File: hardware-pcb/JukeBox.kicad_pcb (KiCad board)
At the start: 2 copper layers, 93.8 x 90 mm, 82 parts, among them J1 USB4105-GF-A, J2 Conn_01x04_Pin, Q1 Q_NPN_BEC, SW1 SW_SPST, SW10 SW_SPST, SW11 SW_SPST, SW12 SW_SPST, SW2 SW_SPST, SW3 SW_SPST, SW4 SW_SPST, SW5 SW_SPST, SW6 SW_SPST, SW7 SW_SPST, SW8 SW_SPST, SW9 SW_SPST, U1 NCP1117-3.3_SOT223, U2 W25Q64JVSSIQ-TR, U3 RP2040, U4 st7789v, U5 CAT24C512, Y1 ECS-120-20-33-AEL-TR

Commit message: minor eeprom updates
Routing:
- net /GPIO4: track 92.0 -> 92.9 mm
- net /GPIO5: track 92.8 -> 93.3 mm
- net GND: vias 35 -> 43
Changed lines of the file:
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@@
 		(tags "SOIC SO")
 		(property "Reference" "U5"
-			(at 0 0 360)
+			(at 0 0 0)
 			(layer "F.SilkS")
 			(effects
@@
 		)
 		(property "Value" "CAT24C512"
-			(at 0 3.4 360)
+			(at 0 3.4 0)
 			(layer "F.Fab")
 			(effects
@@
 		)
 		(fp_text user "${REFERENCE}"
-			(at 0 0 360)
+			(at 0 0 0)
 			(layer "F.Fab")
 			(effects
@@
 	)
 	(via
+		(at 102.59 141.85)
+		(size 0.6)
+		(drill 0.35)
+		(layers "F.Cu" "B.Cu")
+		(free yes)
+		(net 1)
+	)
+	(via
 		(at 112.59 131.85)
 		(size 0.6)
@@
 	)
 	(via
+		(at 122.59 141.85)
+		(size 0.6)
+		(drill 0.35)
+		(layers "F.Cu" "B.Cu")
+		(free yes)
+		(net 1)
+	)
+	(via
 		(at 89.09 94.75)
 		(size 0.6)
@@
 	)
 	(via
+		(at 82.59 121.85)
+		(size 0.6)
+		(drill 0.35)
+		(layers "F.Cu" "B.Cu")
+		(free yes)
+		(net 1)
+	)
+	(via
 		(at 70.09 111.85)
 		(size 0.6)
@@
 	)
 	(via
+		(at 102.59 121.85)
+		(size 0.6)
+		(drill 0.35)
+		(layers "F.Cu" "B.Cu")
+		(free yes)
+		(net 1)
+	)
+	(via
 		(at 155.09 151.85)
 		(size 0.6)
@@
 	)
 	(via
+		(at 82.59 141.85)
+		(size 0.6)
+		(drill 0.35)
+		(layers "F.Cu" "B.Cu")
+		(free yes)
+		(net 1)
+	)
+	(via
 		(at 92.59 131.85)
 		(size 0.6)
@@
 	)
 	(via
+		(at 142.59 141.85)
+		(size 0.6)
+		(drill 0.35)
+		(layers "F.Cu" "B.Cu")
+		(free yes)
+		(net 1)
+	)
+	(via
 		(at 132.59 131.85)
 		(size 0.6)
@@
 	)
 	(via
+		(at 122.59 121.85)
+		(size 0.6)
+		(drill 0.35)
+		(layers "F.Cu" "B.Cu")
+		(free yes)
+		(net 1)
+	)
+	(via
+		(at 142.59 121.85)
+		(size 0.6)
+		(drill 0.35)
+		(layers "F.Cu" "B.Cu")
+		(free yes)
+		(net 1)
+	)
+	(via
 		(at 112.59 111.85)
 		(size 0.6)
@@
 	)
 	(segment
-		(start 82.725 100.865)
+		(start 82.225 100.865)
 		(end 83.615 100.865)
 		(width 0.15)
@@
 	)
 	(segment
-		(start 81.84 101.75)
-		(end 82.725 100.865)
+		(start 75.639999 104.799999)
+		(end 77.540001 104.799999)
 		(width 0.15)
 		(layer "F.Cu")
@@
 	)
 	(segment
-		(start 75.639999 104.799999)
-		(end 77.540001 104.799999)
+		(start 75.34 104.5)
+		(end 75.639999 104.799999)
 		(width 0.15)
 		(layer "F.Cu")
@@
 	)
 	(segment
-		(start 75.34 104.5)
-		(end 75.639999 104.799999)
+		(start 81.34 101.75)
+		(end 82.225 100.865)
 		(width 0.15)
 		(layer "F.Cu")
@@
 	)
 	(via
-		(at 81.84 101.75)
+		(at 81.34 101.75)
 		(size 0.6)
 		(drill 0.35)
@@
 	)
 	(segment
-		(start 81.84 101.75)
-		(end 80.84 102.75)
+		(start 81.34 101.75)
+		(end 80.34 102.75)
 		(width 0.15)
 		(layer "B.Cu")
@@
 	)
 	(segment
-		(start 82.09 101.5)
-		(end 81.84 101.75)
+		(start 147.09 101.5)
+		(end 147.715 100.875)
 		(width 0.15)
 		(layer "B.Cu")
@@
 	)
 	(segment
-		(start 80.84 102.75)
-		(end 79.59 102.75)
+		(start 81.59 101.5)
+		(end 147.09 101.5)
 		(width 0.15)
 		(layer "B.Cu")
@@
 	)
 	(segment
-		(start 147.09 101.5)
-		(end 82.09 101.5)
+		(start 81.34 101.75)
+		(end 81.59 101.5)
 		(width 0.15)
 		(layer "B.Cu")
@@
 	)
 	(segment
-		(start 147.715 100.875)
-		(end 147.09 101.5)
+		(start 80.34 102.75)
+		(end 79.59 102.75)
 		(width 0.15)
 		(layer "B.Cu")
@@
 	)
 	(segment
-		(start 82.745 99.595)
+		(start 81.87 99.595)
 		(end 83.615 99.595)
 		(width 0.15)
@@
 	)
 	(segment
-		(start 81.715 100.625)
-		(end 82.745 99.595)
+		(start 147.84 93.739558)
+		(end 146.49 92.389558)
 		(width 0.15)
 		(layer "F.Cu")
@@
 	)
 	(segment
-		(start 147.84 93.739558)
-		(end 146.49 92.389558)
+		(start 80.84 100.625)
+		(end 81.87 99.595)
 		(width 0.15)
 		(layer "F.Cu")
@@
 	)
 	(via
-		(at 81.715 100.625)
+		(at 80.84 100.625)
 		(size 0.6)
 		(drill 0.35)
@@
 	)
 	(segment
-		(start 147.798436 99.791564)
-		(end 147.798436 99.706248)
+		(start 80.84 100.625)
+		(end 79.24 102.225)
 		(width 0.15)
 		(layer "B.Cu")
@@
 	)
 	(segment
-		(start 82.09 101)
-		(end 146.59 101)
+		(start 147.798436 99.791564)
+		(end 147.798436 99.706248)
 		(width 0.15)
 		(layer "B.Cu")
@@
 	)
 	(segment
-		(start 146.59 101)
-		(end 147.798436 99.791564)
+		(start 79.24 102.225)
+		(end 78.115 102.225)
 		(width 0.15)
 		(layer "B.Cu")
@@
 	)
 	(segment
-		(start 81.715 100.625)
-		(end 80.115 102.225)
+		(start 78.115 102.225)
+		(end 77.59 102.75)
 		(width 0.15)
 		(layer "B.Cu")
@@
 	)
 	(segment
-		(start 81.715 100.625)
-		(end 82.09 101)
+		(start 146.59 101)
+		(end 147.798436 99.791564)
 		(width 0.15)
 		(layer "B.Cu")
@@
 	)
 	(segment
-		(start 80.115 102.225)
-		(end 78.115 102.225)
+		(start 80.84 100.625)
+		(end 81.215 101)
 		(width 0.15)
 		(layer "B.Cu")
@@
 	)
 	(segment
-		(start 78.115 102.225)
-		(end 77.59 102.75)
+		(start 81.215 101)
+		(end 146.59 101)
 		(width 0.15)
 		(layer "B.Cu")

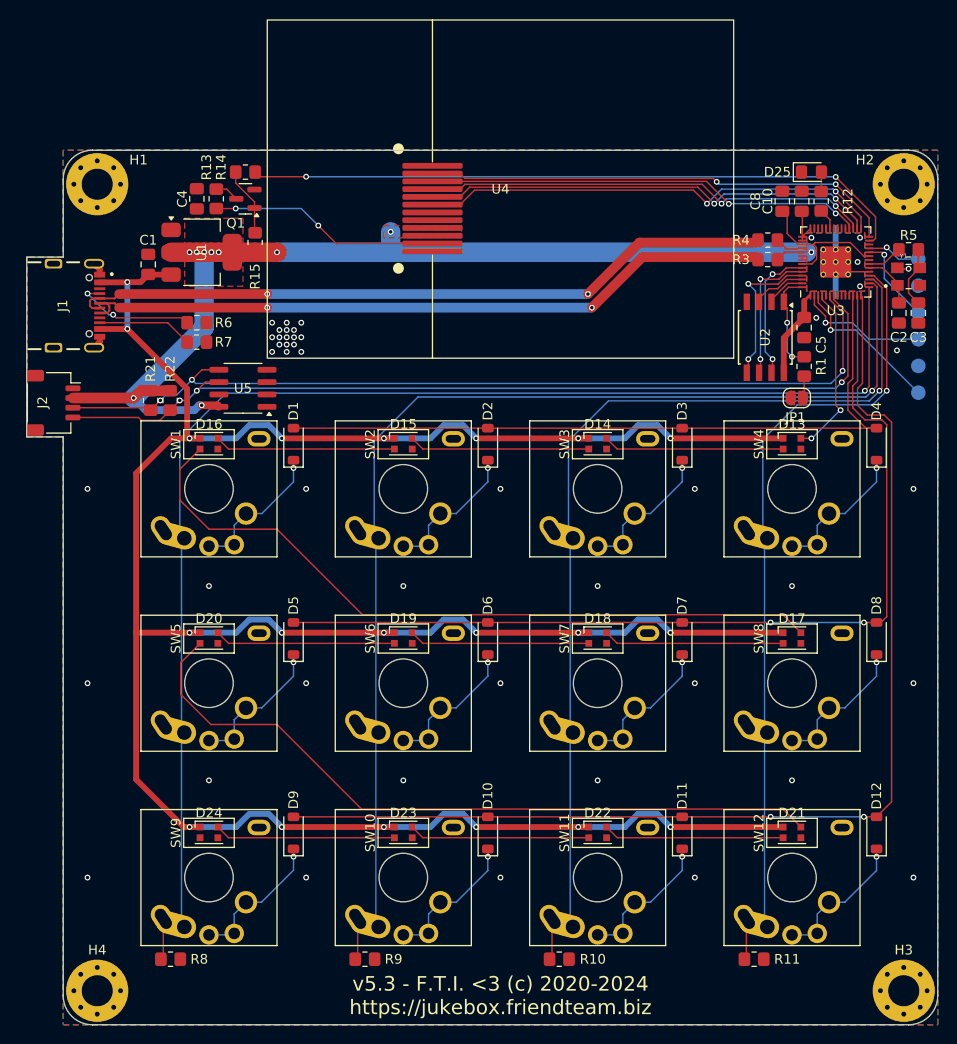
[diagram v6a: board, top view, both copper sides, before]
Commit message: switch to internal kicad usb c, switch to pico clock, fix clock capacitance, fix rgb pinout, fix missing BOM materials
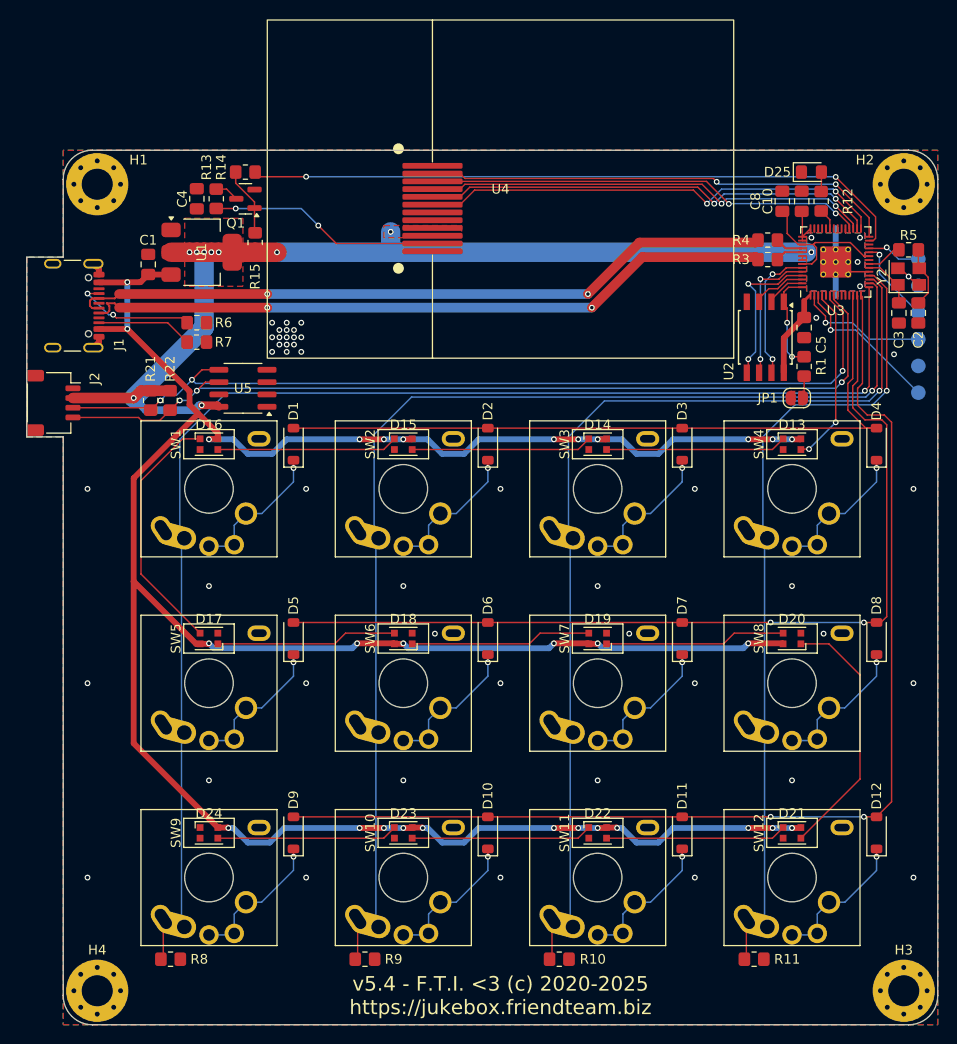
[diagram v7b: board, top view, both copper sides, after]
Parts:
- removed Y1: ECS-120-20-33-AEL-TR, JukeBox:XTAL_ECS-120-20-33-AEL-TR
- added Y2: ABM8-272-T3, Crystal:Crystal_SMD_Abracon_ABM8G-4Pin_3.2x2.5mm, F.Cu at (154.6, 90.0)
- C2, C3: value 27p -> 15p
- J1: value USB4105-GF-A -> USB_C_Receptacle_USB2.0_16P; footprint JukeBox:GCT_USB4105-GF-A -> Connector_USB:USB_C_Receptacle_GCT_USB4105-xx-A_16P_TopMnt_Horizontal
- moved D17 60.0 mm to (82.6, 127.2), turned to 180 degrees
- moved D20 60.0 mm to (142.6, 127.2), turned to 180 degrees
- moved D18 20.0 mm to (102.6, 127.2), turned to 180 degrees
- moved D19 20.0 mm to (122.6, 127.2), turned to 180 degrees
- moved C2 2.00 mm to (155.6, 93.8), turned to 90 degrees
- moved C3 2.00 mm to (153.6, 93.8), turned to -90 degrees
- moved J1 1.00 mm to (67.6, 93.0)
- moved D21 0.05 mm to (142.6, 147.2)
- moved D22 0.05 mm to (122.6, 147.2)
- moved D23 0.05 mm to (102.6, 147.2)
- moved D24 0.05 mm to (82.6, 147.2)
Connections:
- C2 pad 1: /XIN -> GND
- C2 pad 2: GND -> Net-(C2-Pad2)
- C3 pad 1: GND -> /XIN
- C3 pad 2: Net-(Y1-OUT/IN) -> GND
- D13 pad 1: VBUS -> Net-(D13-DOUT)
- D13 pad 2: Net-(D13-DOUT) -> GND
- D13 pad 3: GND -> /GPIO2
- D13 pad 4: /GPIO2 -> VBUS
- D14 pad 1: VBUS -> Net-(D14-DOUT)
- D14 pad 2: Net-(D14-DOUT) -> GND
- D14 pad 3: GND -> Net-(D13-DOUT)
- D14 pad 4: Net-(D13-DOUT) -> VBUS
- D15 pad 1: VBUS -> Net-(D15-DOUT)
- D15 pad 2: Net-(D15-DOUT) -> GND
- D15 pad 3: GND -> Net-(D14-DOUT)
- D15 pad 4: Net-(D14-DOUT) -> VBUS
- D16 pad 1: VBUS -> Net-(D16-DOUT)
- D16 pad 2: Net-(D16-DOUT) -> GND
- D16 pad 3: GND -> Net-(D15-DOUT)
- D16 pad 4: Net-(D15-DOUT) -> VBUS
- D17 pad 1: VBUS -> Net-(D17-DOUT)
- D17 pad 2: Net-(D17-DOUT) -> GND
- D17 pad 3: GND -> Net-(D16-DOUT)
- D17 pad 4: Net-(D16-DOUT) -> VBUS
- D18 pad 1: VBUS -> Net-(D18-DOUT)
- D18 pad 2: Net-(D18-DOUT) -> GND
- D18 pad 3: GND -> Net-(D17-DOUT)
- D18 pad 4: Net-(D17-DOUT) -> VBUS
- D19 pad 1: VBUS -> Net-(D19-DOUT)
- D19 pad 2: Net-(D19-DOUT) -> GND
- D19 pad 3: GND -> Net-(D18-DOUT)
- D19 pad 4: Net-(D18-DOUT) -> VBUS
- D20 pad 1: VBUS -> Net-(D20-DOUT)
- D20 pad 2: Net-(D20-DOUT) -> GND
- D20 pad 3: GND -> Net-(D19-DOUT)
- D20 pad 4: Net-(D19-DOUT) -> VBUS
- D21 pad 1: VBUS -> Net-(D21-DOUT)
- D21 pad 2: Net-(D21-DOUT) -> GND
- D21 pad 3: GND -> Net-(D20-DOUT)
- D21 pad 4: Net-(D20-DOUT) -> VBUS
- D22 pad 1: VBUS -> Net-(D22-DOUT)
- D22 pad 2: Net-(D22-DOUT) -> GND
- D22 pad 3: GND -> Net-(D21-DOUT)
- D22 pad 4: Net-(D21-DOUT) -> VBUS
- D23 pad 1: VBUS -> Net-(D23-DOUT)
- D23 pad 2: Net-(D23-DOUT) -> GND
- D23 pad 3: GND -> Net-(D22-DOUT)
- D23 pad 4: Net-(D22-DOUT) -> VBUS
- D24 pad 1: VBUS -> /RGBDOUT
- D24 pad 2: /RGBDOUT -> GND
- D24 pad 3: GND -> Net-(D23-DOUT)
- D24 pad 4: Net-(D23-DOUT) -> VBUS
- J2 pad MP: GND -> (no net)
- R5 pad 2: Net-(Y1-OUT/IN) -> Net-(C2-Pad2)
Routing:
- net Net-(D16-DOUT): track 75.7 -> 26.1 mm
- net Net-(D20-DOUT): track 75.5 -> 26.7 mm
- net Net-(Y1-OUT/IN): track 6.42 -> 0.00 mm
- net Net-(C2-Pad2): track 0.00 -> 6.31 mm
- net VBUS: track 283.9 -> 281.8 mm, vias 20 -> 30
- net GND: track 33.1 -> 34.9 mm, vias 43 -> 46
- net /USB_D+: track 72.9 -> 71.5 mm
- net /GPIO2: track 17.9 -> 18.4 mm
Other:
- board text added: "v5.4 - F.T.I. <3 (c) 2020-2025 https://jukebox.friendteam.biz"
- board text removed: "v5.3 - F.T.I. <3 (c) 2020-2024 https://jukebox.friendteam.biz"

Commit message: switch from 0805 to 0402
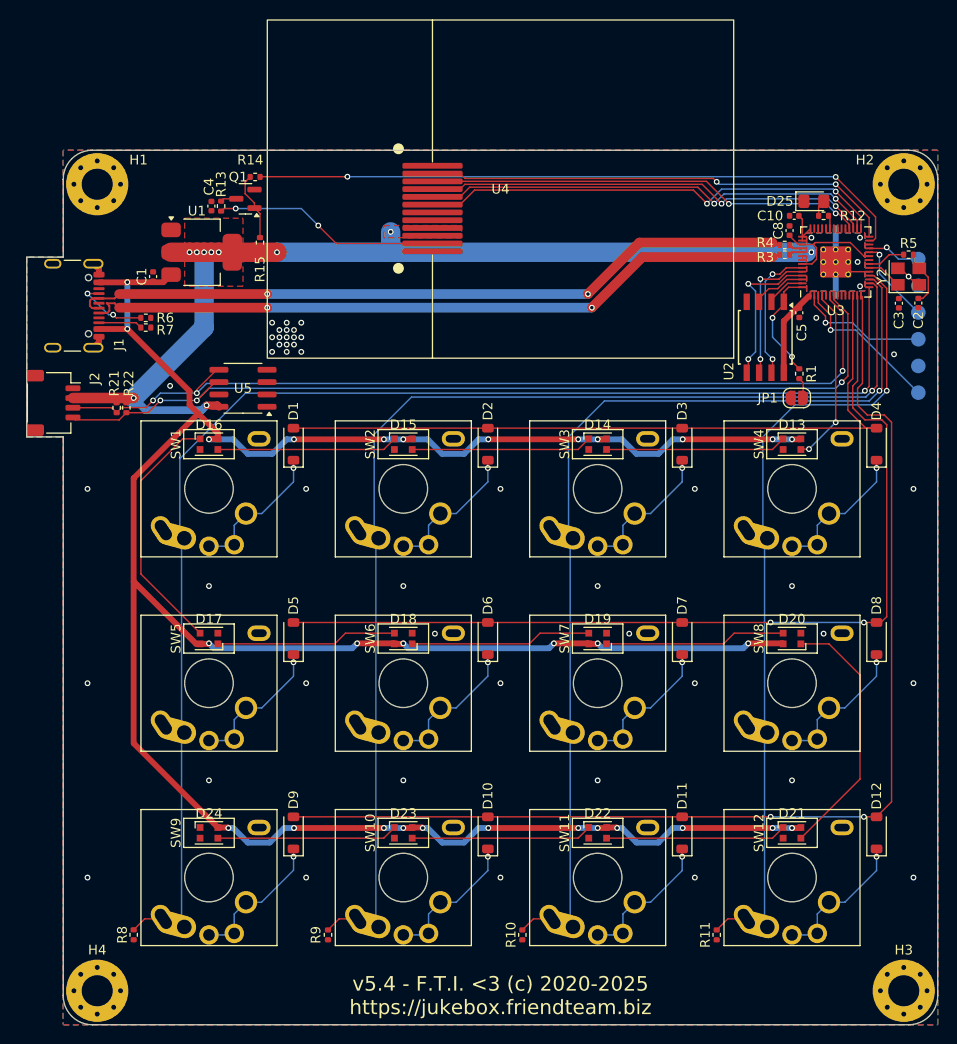
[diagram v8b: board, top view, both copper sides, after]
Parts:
- C1, C10, C2, C3, C4, C5, C8: footprint Capacitor_SMD:C_0805_2012Metric_Pad1.18x1.45mm_HandSolder -> Capacitor_SMD:C_0402_1005Metric
- R1, R10, R11, R12, R13, R14, R15, R21, R22, R3, R4, R5, R6, R7, R8, R9: footprint Resistor_SMD:R_0805_2012Metric_Pad1.20x1.40mm_HandSolder -> Resistor_SMD:R_0402_1005Metric
- moved R7 5.46 mm to (76.1, 95.2)
- moved R6 5.27 mm to (76.1, 94.2)
- moved R11 4.59 mm to (134.8, 157.8), turned to 90 degrees
- moved R22 4.56 mm to (74.1, 103.5)
- moved R8 4.55 mm to (74.8, 157.7), turned to 90 degrees
- moved R10 4.55 mm to (114.8, 157.8), turned to 90 degrees
- moved R9 4.55 mm to (94.8, 157.8), turned to 90 degrees
- moved R21 3.58 mm to (73.1, 103.5)
- moved C8 3.11 mm to (142.3, 85.3)
- moved D25 3.01 mm to (144.8, 82.2)
- moved R3 1.82 mm to (141.8, 87.8)
- moved R4 1.82 mm to (141.8, 86.8)
- moved C10 1.69 mm to (142.8, 83.8), turned to 180 degrees
- moved C4 1.68 mm to (82.8, 82.8)
- moved C5 1.60 mm to (143.3, 93.7)
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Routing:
- net Net-(J1-CC2): track 9.90 -> 4.52 mm
- net Net-(J1-CC1): track 12.7 -> 7.71 mm
- net +3V3: track 123.4 -> 119.0 mm
- net +1V1: track 15.4 -> 12.6 mm
- net /USB_D-: track 72.9 -> 75.1 mm
- net /USB_D+: track 71.5 -> 73.8 mm
- net /GPIO12: track 138.5 -> 136.6 mm
- net /XIN: track 5.55 -> 3.83 mm
- net /USB_R_D-: track 2.91 -> 1.45 mm
- net /USB_R_D+: track 2.87 -> 1.41 mm
- net /QSPI_SS: track 10.4 -> 11.6 mm
- net Net-(Q1-C): track 2.48 -> 1.66 mm
- net /GPIO25: track 2.19 -> 1.37 mm
- net /GPIO14: track 101.7 -> 101.0 mm
- net /GPIO13: track 120.6 -> 119.8 mm
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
